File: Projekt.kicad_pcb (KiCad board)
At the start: 2 copper layers, 93.5 x 60.8 mm, 118 parts, among them J1 Solar, J2 Battery, J3 USB_B_Mini, J4 INTERFACE PORT, J5 FAN, J6 JTAG, J7 PRG, J8 Micro_SD_Card_Det_Hirose_DM3AT, J9 IIC RTC, Q1 CSD19505KCS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

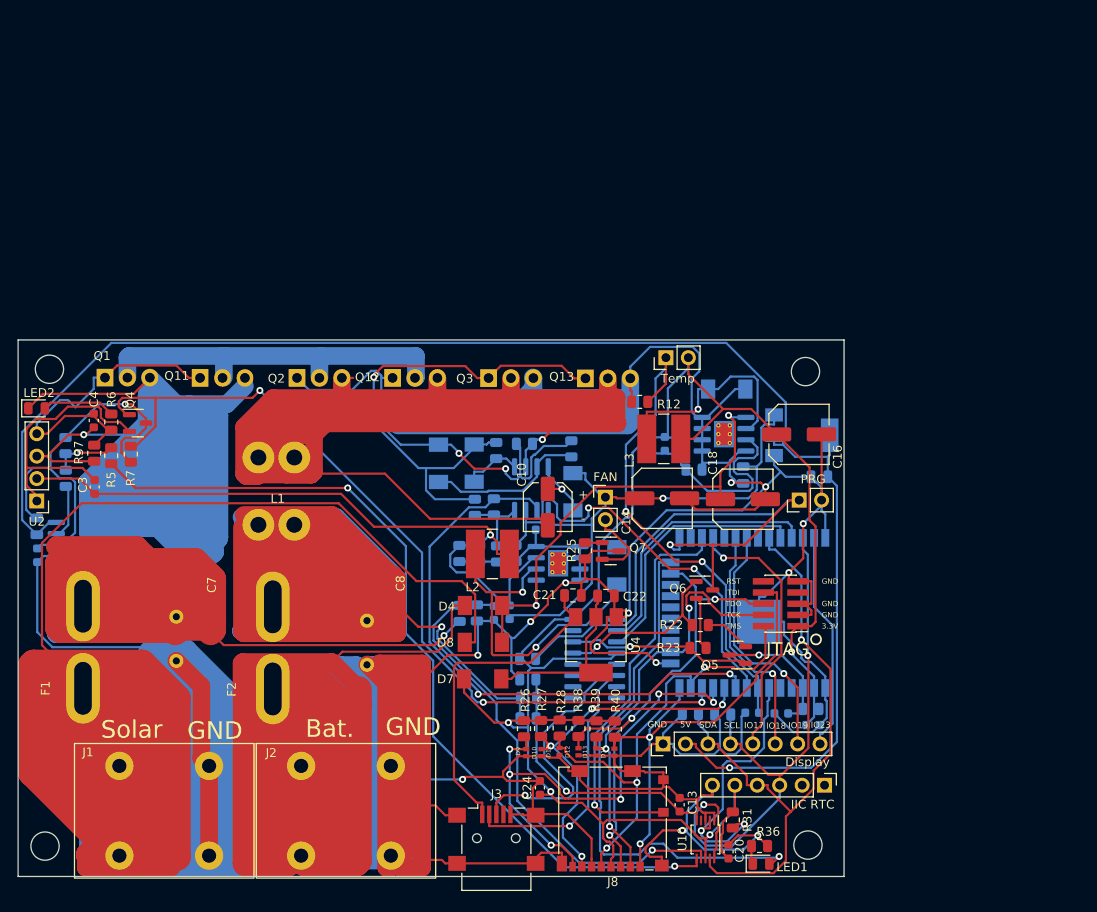
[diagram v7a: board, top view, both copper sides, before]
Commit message: 3D Modelle und Footprints vervollständigt
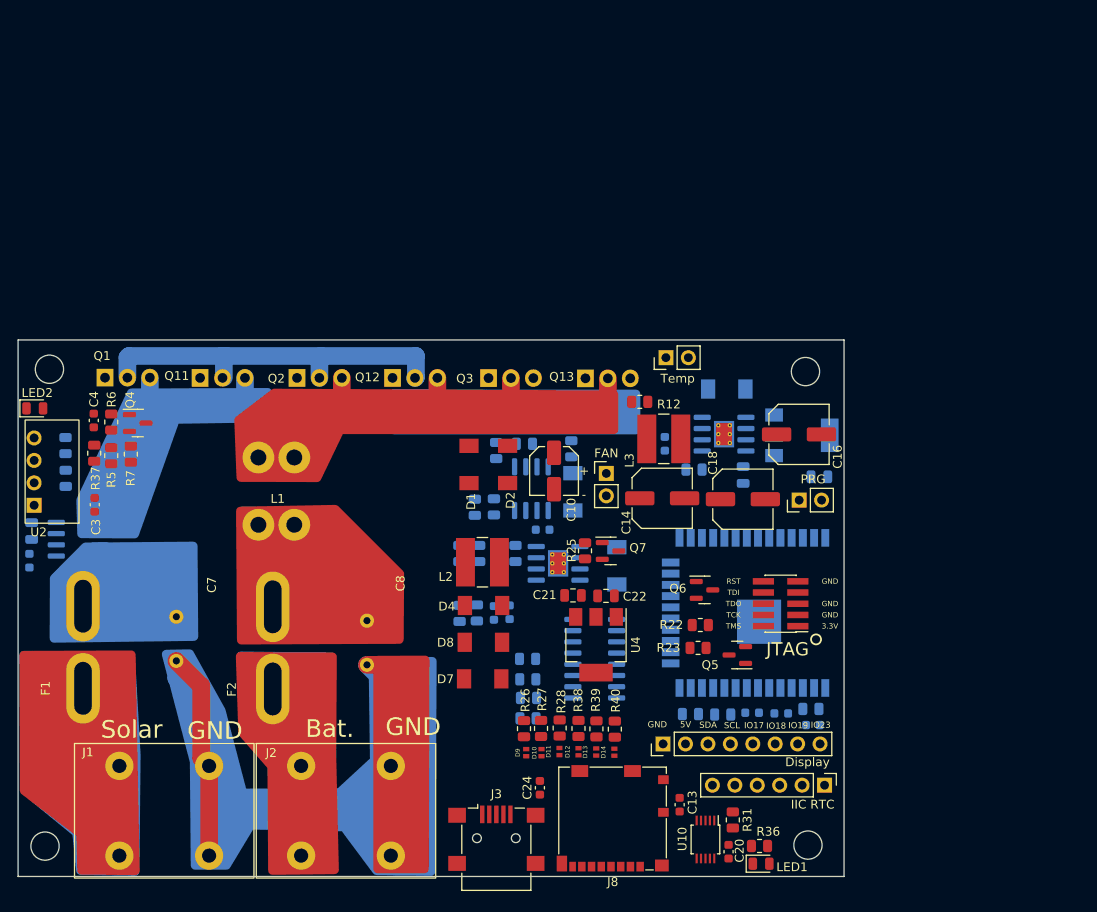
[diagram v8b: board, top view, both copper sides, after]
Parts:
- added JP1: Copper Bar, AA:COPPER_BAR, B.Cu at (122.9, 127.3)
- D1, D2: moved to F.Cu
- U2: footprint Connector_PinHeader_2.54mm:PinHeader_1x04_P2.54mm_Vertical -> AA:B1212S
- moved C10 4.15 mm to (139.1, 109.0)
- moved D2 3.79 mm to (133.9, 108.3)
- moved D1 3.46 mm to (129.5, 108.3)
- moved J5 2.69 mm to (145.1, 109.3)
- moved C3 2.00 mm to (87.1, 112.8)
- moved L2 1.47 mm to (131.0, 119.4)
- moved C2 1.08 mm to (79.7, 119.2)
- moved C9 0.79 mm to (80.0, 115.8)
- moved U2 0.57 mm to (80.3, 112.9)
- moved LED2 0.21 mm to (80.3, 101.9)
- turned D9 to -90 degrees
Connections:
- D9 pad 1: GND -> GPIO26
- D9 pad 2: GPIO26 -> GND
- J2 pad 2: GND -> Net-(J2-Pad2)
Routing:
- net GND: track 1072.6 -> 95.3 mm, vias 13 -> 0
- net Net-(D8-Pad2): track 464.8 -> 31.1 mm
- net Net-(C8-Pad1): track 356.1 -> 69.5 mm, vias 1 -> 0
- net Net-(C7-Pad1): track 262.0 -> 18.8 mm, vias 1 -> 0
- net +3.3V: track 201.9 -> 0.00 mm, vias 4 -> 0
- net Net-(D4-Pad2): track 214.5 -> 30.2 mm
- net +5V: track 176.1 -> 0.00 mm, vias 1 -> 0
- net Net-(C10-Pad2): track 216.7 -> 56.7 mm, vias 1 -> 0
- net Net-(C4-Pad2): track 182.1 -> 33.0 mm, vias 1 -> 0
- net +12V: track 137.6 -> 0.00 mm, vias 2 -> 0
- net GPIO27: track 98.2 -> 0.00 mm, vias 3 -> 0
- net A2: track 97.0 -> 0.00 mm, vias 2 -> 0
- net SDA: track 69.7 -> 0.00 mm, vias 1 -> 0
- net GPIO0: track 66.0 -> 0.00 mm, vias 1 -> 0
- net GPIO33: track 65.8 -> 0.00 mm, vias 2 -> 0
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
